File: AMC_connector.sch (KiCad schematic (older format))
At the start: 2 parts, among them P1 CMP-0001-00058-2

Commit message: LEDs and button added, routed other signals
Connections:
- net labels added: 3V3PM
- net labels removed: +3V3MP
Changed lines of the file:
@@
 Wire Wire Line
 	9200 4700 9700 4700
-$Comp
-L power2:+3V3MP #PWR030
-U 1 1 5BFC5E93
-P 1950 6700
-AR Path="/5BD320D5/5BFC5E93" Ref="#PWR030"  Part="1"
-AR Path="/5C16BF8E/5BFC5E93" Ref="#PWR030"  Part="1"
-F 0 "#PWR030" H 1950 6550 50  0001 C CNN
-F 1 "+3V3MP" H 1965 6873 50  0000 C CNN
-F 2 "" H 1950 6700 50  0001 C CNN
-F 3 "" H 1950 6700 50  0001 C CNN
-	1    1950 6700
-	1    0    0    -1
-$EndComp
 Wire Wire Line
 	1950 6700 1950 7700
@@
 	1    0    0    -1
 $EndComp
-Wire Wire Line
-	2450 7700 2450 6500
 $Comp
 L AMC_FMC_Carrier-PcbDoc-rescue:+12V_AMC-powerMG #PWR033
@@
 Wire Wire Line
 	3800 4450 4150 4450
+$Comp
+L power:+3.3VP #PWR0631
+U 1 1 5D7C0506
+P 1950 6700
+F 0 "#PWR0631" H 1955 6840 50  0001 C CNN
+F 1 "3V3PM" H 1935 6873 50  0000 C CNN
+F 2 "" H 1950 6700 50  0001 C CNN
+F 3 "" H 1950 6700 50  0001 C CNN
+	1    1950 6700
+	1    0    0    -1
+$EndComp
+Wire Wire Line
+	2450 6500 2450 7700
 Wire Bus Line
 	10026 4346 10026 4546

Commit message: routing finished
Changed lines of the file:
@@
 Text Label 7150 7493 1    60   ~ 12
 IPMB_SCL
-Text Label 8650 7493 1    60   ~ 12
+Text Label 8650 7500 1    60   ~ 12
 IPMB_SDA
-Text Label 8950 7493 1    60   ~ 12
+Text Label 8950 7500 1    60   ~ 12
 TCLKA_P
-Text Label 9050 7493 1    60   ~ 12
+Text Label 9050 7500 1    60   ~ 12
 TCLKA_N
-Text Label 9250 7493 1    60   ~ 12
+Text Label 9250 7500 1    60   ~ 12
 TCLKB_P
-Text Label 9350 7493 1    60   ~ 12
+Text Label 9350 7500 1    60   ~ 12
 TCLKB_N
-Text Label 9550 7493 1    60   ~ 12
+Text Label 9550 7500 1    60   ~ 12
 FCLKA_P
-Text Label 9650 7493 1    60   ~ 12
+Text Label 9650 7500 1    60   ~ 12
 FCLKA_N
 Text Label 9850 7493 1    60   ~ 12
@@
 Text Label 3950 9243 1    60   ~ 12
 Tx11_P
-Text Label 6550 9143 1    60   ~ 12
+Text Label 6550 9100 1    60   ~ 12
 TCLKC_N
-Text Label 6650 9143 1    60   ~ 12
+Text Label 6650 9100 1    60   ~ 12
 TCLKC_P
-Text Label 6850 9143 1    60   ~ 12
+Text Label 6850 9150 1    60   ~ 12
 TCLKD_N
-Text Label 6950 9143 1    60   ~ 12
+Text Label 6950 9150 1    60   ~ 12
 TCLKD_P
 Text Label 7150 9143 1    60   ~ 12

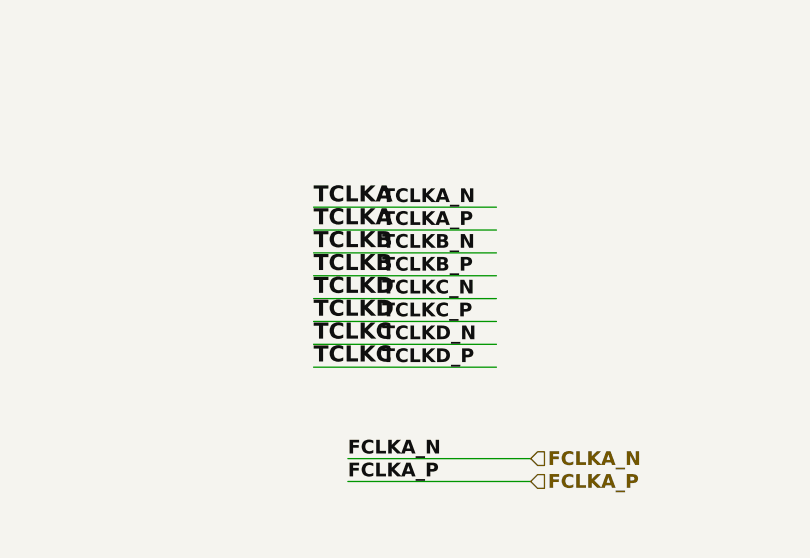
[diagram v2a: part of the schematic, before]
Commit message: HDMI footprint changed, silk layer edited, bugs fixed
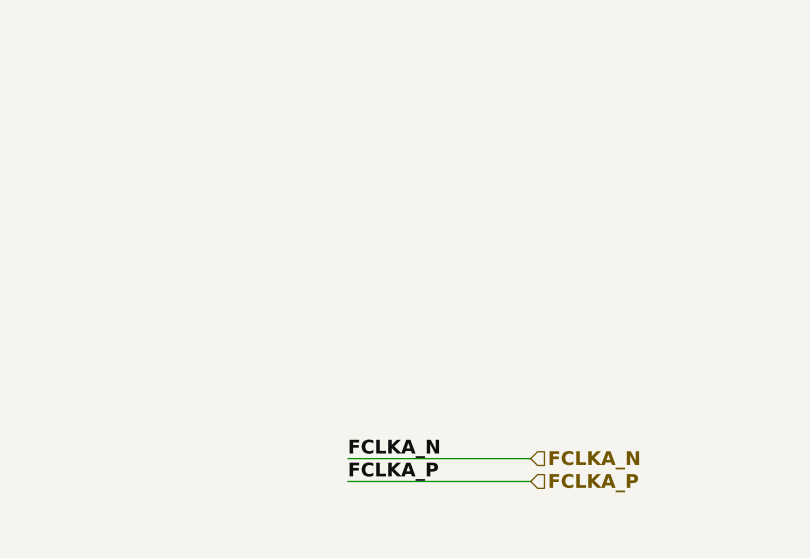
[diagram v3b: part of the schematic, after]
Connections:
- net labels removed: TCLKA, TCLKB, TCLKC, TCLKD
- wire segments 334 -> 326
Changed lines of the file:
@@
 Text Label 9050 7500 1    60   ~ 12
 TCLKA_N
-Text Label 9250 7500 1    60   ~ 12
-TCLKB_P
-Text Label 9350 7500 1    60   ~ 12
-TCLKB_N
-Text Label 9550 7500 1    60   ~ 12
-FCLKA_P
-Text Label 9650 7500 1    60   ~ 12
-FCLKA_N
 Text Label 9850 7493 1    60   ~ 12
 PS0#
@@
 Text Label 3950 9243 1    60   ~ 12
 Tx11_P
-Text Label 6550 9100 1    60   ~ 12
-TCLKC_N
-Text Label 6650 9100 1    60   ~ 12
-TCLKC_P
-Text Label 6850 9150 1    60   ~ 12
-TCLKD_N
-Text Label 6950 9150 1    60   ~ 12
-TCLKD_P
 Text Label 7150 9143 1    60   ~ 12
 Rx17_N
@@
 	9150 6893 9150 7700
 Wire Wire Line
-	9250 6893 9250 7700
-Wire Wire Line
-	9350 6893 9350 7700
-Wire Wire Line
 	9450 6893 9450 7700
 Wire Wire Line
-	9550 6893 9550 7700
-Wire Wire Line
-	9650 6893 9650 7700
-Wire Wire Line
 	9750 6893 9750 7700
 Wire Wire Line
@@
 	7050 8500 7050 9343
 Wire Wire Line
-	6950 8500 6950 9343
-Wire Wire Line
-	6850 8500 6850 9343
-Wire Wire Line
 	6750 8500 6750 9343
-Wire Wire Line
-	6650 8500 6650 9343
-Wire Wire Line
-	6550 8500 6550 9343
 Wire Wire Line
 	6450 8500 6450 9343
@@
 	1    0    0    -1
 $EndComp
-Text Label 9364 1433 0    60   ~ 12
-TCLKA_N
-Text Label 9364 1533 0    60   ~ 12
-TCLKA_P
-Text Label 9364 1633 0    60   ~ 12
-TCLKB_N
-Text Label 9364 1733 0    60   ~ 12
-TCLKB_P
-Text Label 9364 1833 0    60   ~ 12
-TCLKC_N
-Text Label 9364 1933 0    60   ~ 12
-TCLKC_P
-Text Label 9364 2033 0    60   ~ 12
-TCLKD_N
-Text Label 9364 2133 0    60   ~ 12
-TCLKD_P
 Text Label 9214 2533 0    60   ~ 12
 FCLKA_N
-Text Label 9064 1433 0    70   ~ 14
-TCLKA
-Text Label 9064 1533 0    70   ~ 14
-TCLKA
-Text Label 9064 1633 0    70   ~ 14
-TCLKB
-Text Label 9064 1733 0    70   ~ 14
-TCLKB
-Text Label 9064 2033 0    70   ~ 14
-TCLKC
-Text Label 9064 2133 0    70   ~ 14
-TCLKC
-Text Label 9064 1833 0    70   ~ 14
-TCLKD
-Text Label 9064 1933 0    70   ~ 14
-TCLKD
-Wire Wire Line
-	9864 1433 9064 1433
-Wire Wire Line
-	9864 1533 9064 1533
-Wire Wire Line
-	9864 1633 9064 1633
-Wire Wire Line
-	9864 1733 9064 1733
-Wire Wire Line
-	9864 1833 9064 1833
-Wire Wire Line
-	9864 1933 9064 1933
-Wire Wire Line
-	9864 2033 9064 2033
-Wire Wire Line
-	9864 2133 9064 2133
 Wire Wire Line
 	10014 2533 9214 2533
@@
 Wire Wire Line
 	2450 6500 2450 7700
+Wire Wire Line
+	9650 6893 9650 7700
+Wire Wire Line
+	9550 6893 9550 7700
+Text Label 9650 7500 1    60   ~ 12
+FCLKA_N
+Text Label 9550 7500 1    60   ~ 12
+FCLKA_P
+Wire Wire Line
+	9350 6893 9350 7700
+Wire Wire Line
+	9250 6893 9250 7700
+Text Label 9350 7500 1    60   ~ 12
+TCLKB_N
+Text Label 9250 7500 1    60   ~ 12
+TCLKB_P
+Wire Wire Line
+	6850 8500 6850 9343
+Wire Wire Line
+	6950 8500 6950 9343
+Wire Wire Line
+	6550 8500 6550 9343
+Wire Wire Line
+	6650 8500 6650 9343
+Text Label 6650 9100 1    60   ~ 12
+TCLKC_P
+Text Label 6550 9100 1    60   ~ 12
+TCLKC_N
+Text Label 6850 9150 1    60   ~ 12
+TCLKD_N
+Text Label 6950 9150 1    60   ~ 12
+TCLKD_P
 Wire Bus Line
 	10026 4346 10026 4546

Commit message: bugs fixed, silkscreen edited
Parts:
- renumbered P1 to P3
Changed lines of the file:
@@
 P 1550 7900
 AR Path="/5BD3210B" Ref="P?"  Part="1"
-AR Path="/5BD320D5/5BD3210B" Ref="P1"  Part="1"
-F 0 "P1" H 1520 7753 60  0000 R CNN
+AR Path="/5BD320D5/5BD3210B" Ref="P3"  Part="1"
+F 0 "P3" H 1520 7753 60  0000 R CNN
 F 1 "CMP-0001-00058-2" H 1520 7647 60  0000 R CNN
 F 2 "moja:AMC-GF-2D-750-O274" H 1550 7900 60  0001 C CNN

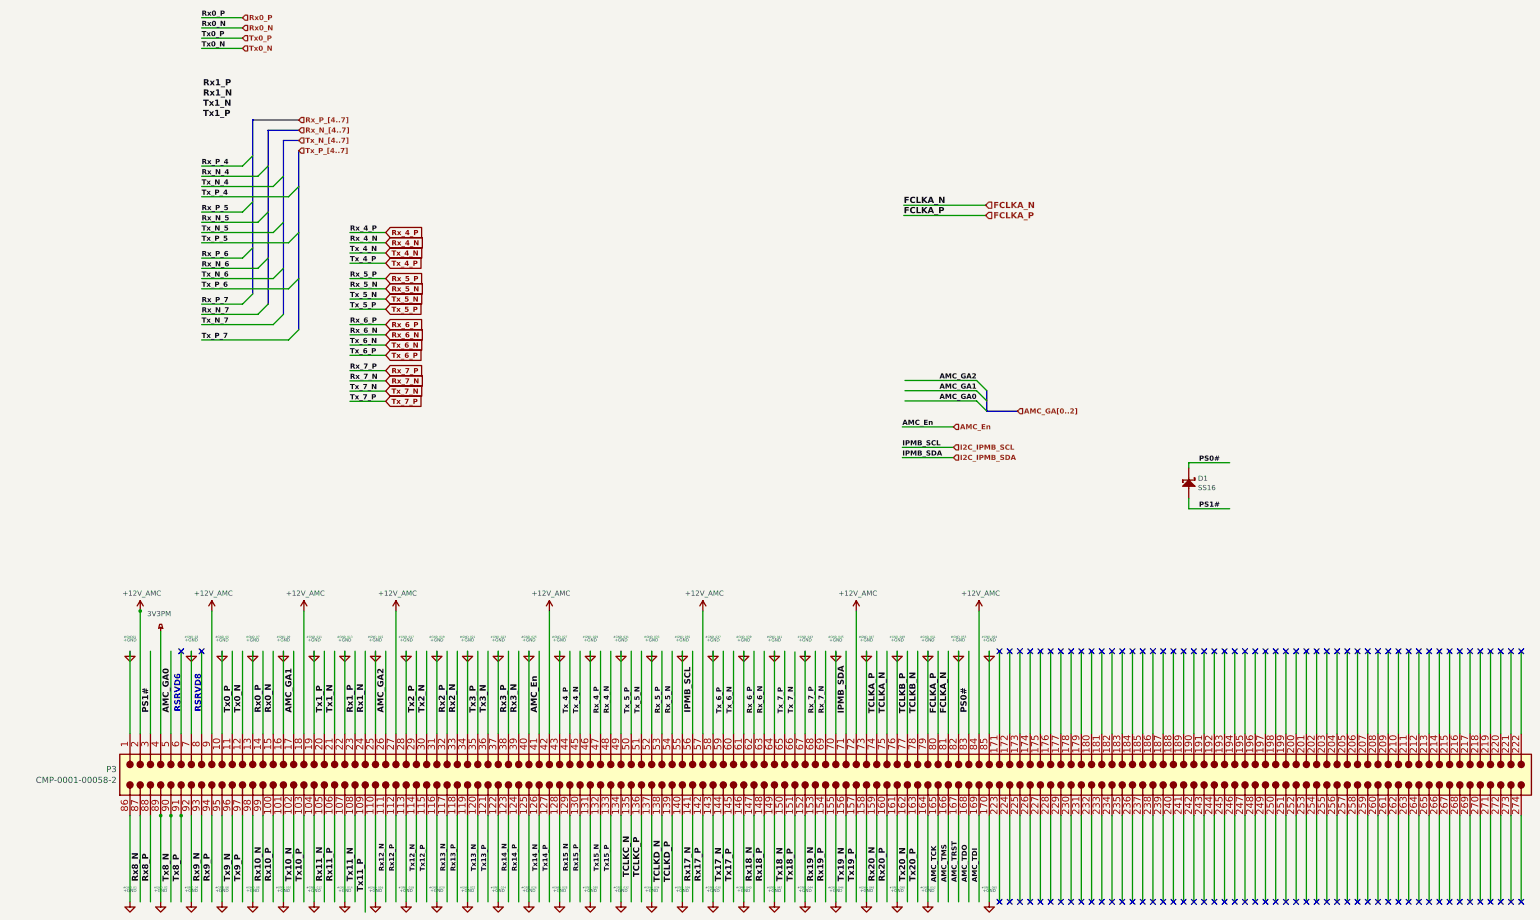
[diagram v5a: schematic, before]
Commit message: new FMC JTAG chain
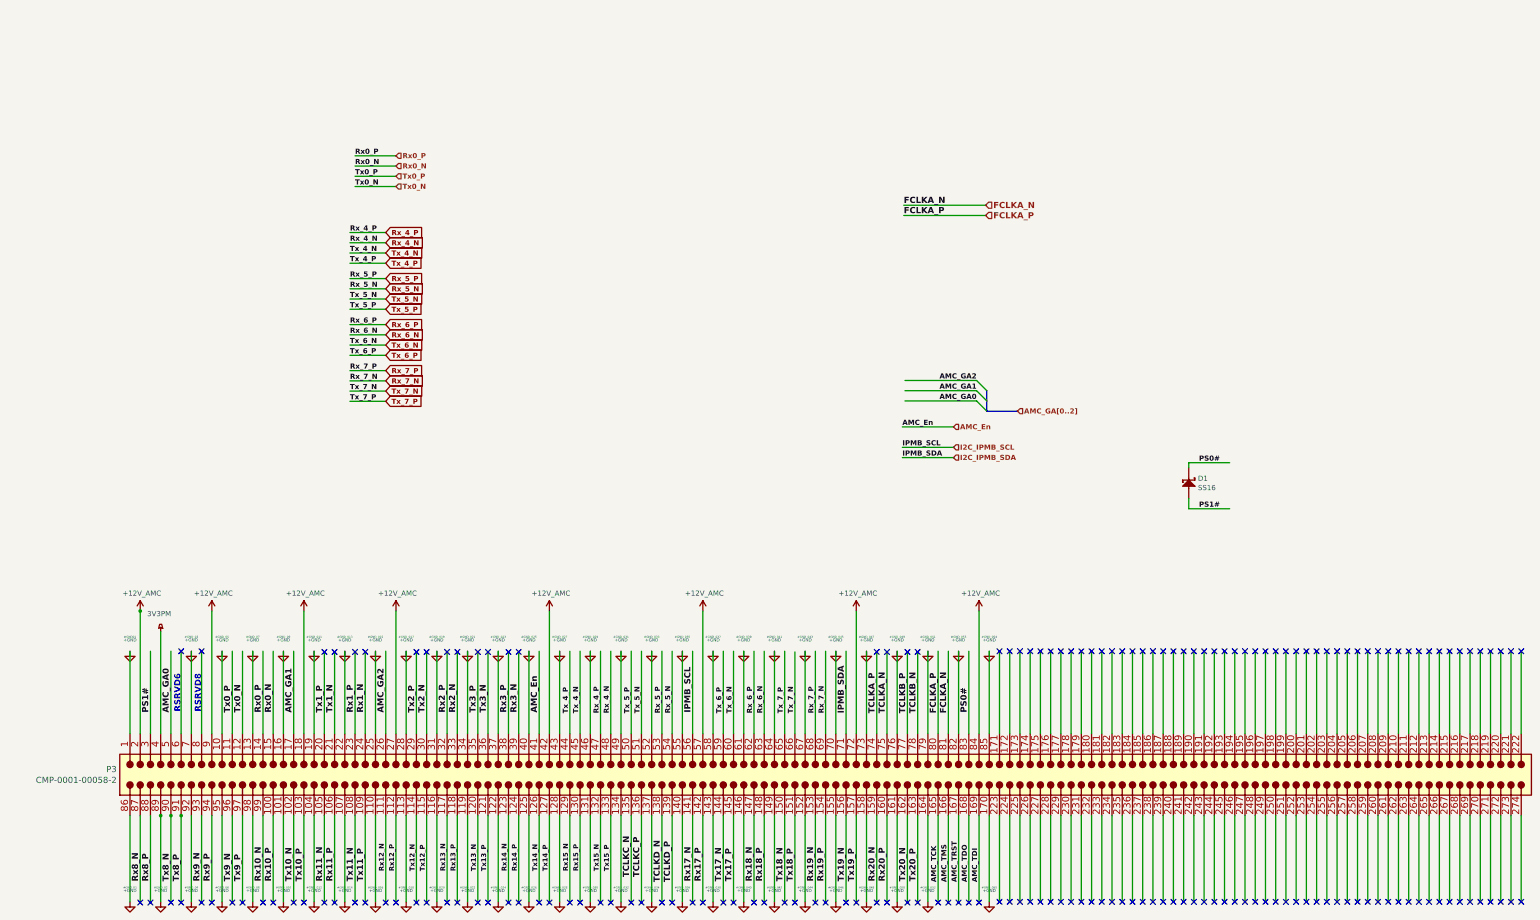
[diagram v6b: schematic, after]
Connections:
- net labels removed: Rx_N_4, Rx_N_5, Rx_N_6, Rx_N_7, Rx_N_[4..7], Rx_P_4, Rx_P_5, Rx_P_6, Rx_P_7, Rx_P_[4..7], Tx_N_4, Tx_N_5, Tx_N_6, Tx_N_7, Tx_N_[4..7], Tx_P_4, Tx_P_5, Tx_P_6, Tx_P_7, Tx_P_[4..7]
- wire segments 326 -> 310
- no-connect marks 106 -> 179

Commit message: BOM updated, 25MHz clock level fixed
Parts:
- P3: symbol AMC_FMC_Carrier-PcbDoc-rescue:CMP-0001-00058-2-AMC -> AMC_FMC_Carrier-PcbDoc-rescue:CMP-0001-00058-2-AMC-AMC_FMC_Carrier-PcbDoc-rescue
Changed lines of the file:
@@
 $EndDescr
 $Comp
-L AMC_FMC_Carrier-PcbDoc-rescue:CMP-0001-00058-2-AMC P?
+L AMC_FMC_Carrier-PcbDoc-rescue:CMP-0001-00058-2-AMC-AMC_FMC_Carrier-PcbDoc-rescue P?
 U 1 1 5BD3210B
 P 1550 7900
@@
 Tx_7_P
 $Comp
-L AMC_FMC_Carrier-PcbDoc-rescue:+12V_AMC-powerMG #PWR029
+L AMC_FMC_Carrier-PcbDoc-rescue:+12V_AMC-powerMG-AMC_FMC_Carrier-PcbDoc-rescue #PWR029
 U 1 1 5DEC6F0B
 P 1750 6500
@@
 	1750 6500 1750 7700
 $Comp
-L AMC_FMC_Carrier-PcbDoc-rescue:+12V_AMC-powerMG #PWR031
+L AMC_FMC_Carrier-PcbDoc-rescue:+12V_AMC-powerMG-AMC_FMC_Carrier-PcbDoc-rescue #PWR031
 U 1 1 5DF1FECB
 P 2450 6500
@@
 $EndComp
 $Comp
-L AMC_FMC_Carrier-PcbDoc-rescue:+12V_AMC-powerMG #PWR032
+L AMC_FMC_Carrier-PcbDoc-rescue:+12V_AMC-powerMG-AMC_FMC_Carrier-PcbDoc-rescue #PWR032
 U 1 1 5DF4CACF
 P 3350 6500
@@
 $EndComp
 $Comp
-L AMC_FMC_Carrier-PcbDoc-rescue:+12V_AMC-powerMG #PWR033
+L AMC_FMC_Carrier-PcbDoc-rescue:+12V_AMC-powerMG-AMC_FMC_Carrier-PcbDoc-rescue #PWR033
 U 1 1 5DFD25BA
 P 4250 6500
@@
 $EndComp
 $Comp
-L AMC_FMC_Carrier-PcbDoc-rescue:+12V_AMC-powerMG #PWR034
+L AMC_FMC_Carrier-PcbDoc-rescue:+12V_AMC-powerMG-AMC_FMC_Carrier-PcbDoc-rescue #PWR034
 U 1 1 5DFFEFC3
 P 5750 6500
@@
 $EndComp
 $Comp
-L AMC_FMC_Carrier-PcbDoc-rescue:+12V_AMC-powerMG #PWR035
+L AMC_FMC_Carrier-PcbDoc-rescue:+12V_AMC-powerMG-AMC_FMC_Carrier-PcbDoc-rescue #PWR035
 U 1 1 5E02B9CC
 P 7250 6500
@@
 $EndComp
 $Comp
-L AMC_FMC_Carrier-PcbDoc-rescue:+12V_AMC-powerMG #PWR036
+L AMC_FMC_Carrier-PcbDoc-rescue:+12V_AMC-powerMG-AMC_FMC_Carrier-PcbDoc-rescue #PWR036
 U 1 1 5E0583D5
 P 8750 6500
@@
 $EndComp
 $Comp
-L AMC_FMC_Carrier-PcbDoc-rescue:+12V_AMC-powerMG #PWR037
+L AMC_FMC_Carrier-PcbDoc-rescue:+12V_AMC-powerMG-AMC_FMC_Carrier-PcbDoc-rescue #PWR037
 U 1 1 5E084DDE
 P 9950 6500
